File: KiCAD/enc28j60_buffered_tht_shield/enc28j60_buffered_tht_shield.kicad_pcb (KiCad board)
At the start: 2 copper layers, 68.6 x 53.3 mm, 8 parts, among them P1 Power, P2 Analog, P3 Digital, P4 Digital, P5 CONN_01X01, P6 CONN_01X01, P7 CONN_01X01, P8 CONN_01X01

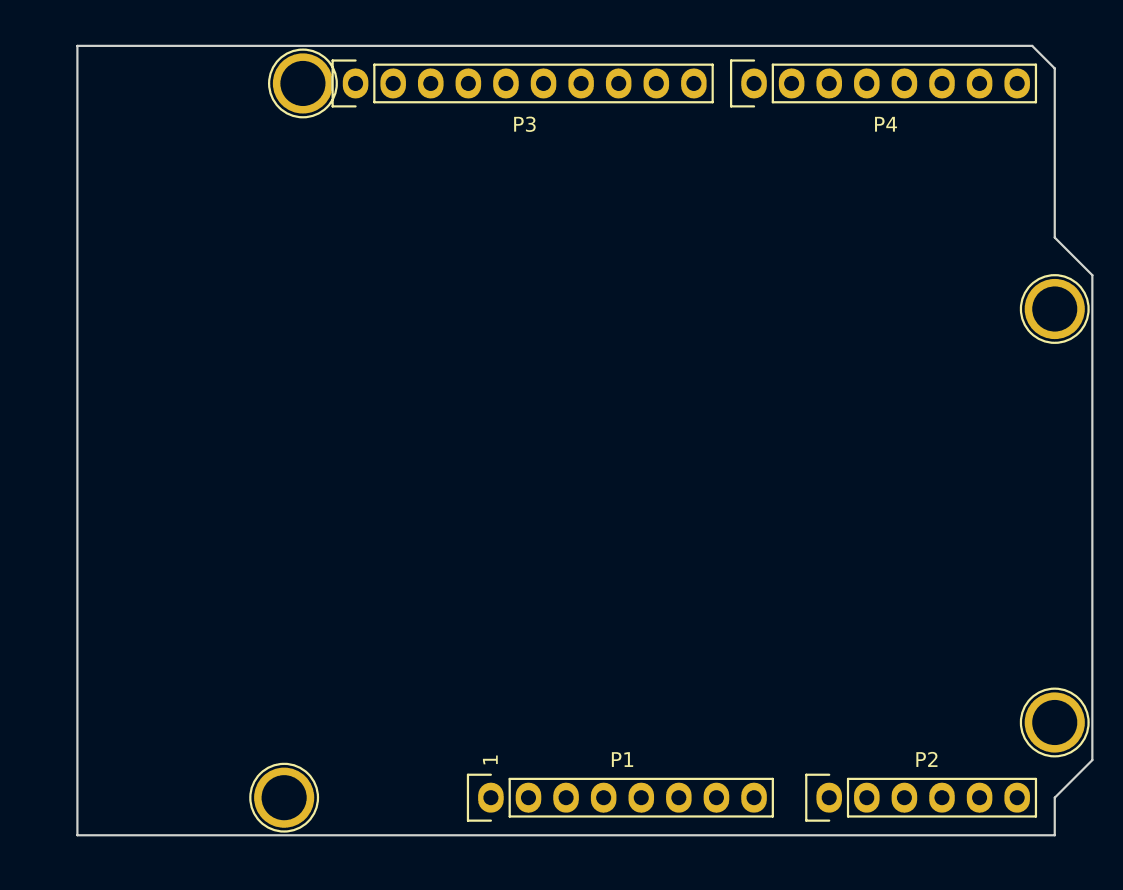
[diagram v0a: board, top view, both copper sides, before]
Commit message: Revision 1. 74HCT125N LM1117 3.3 ENC28J60
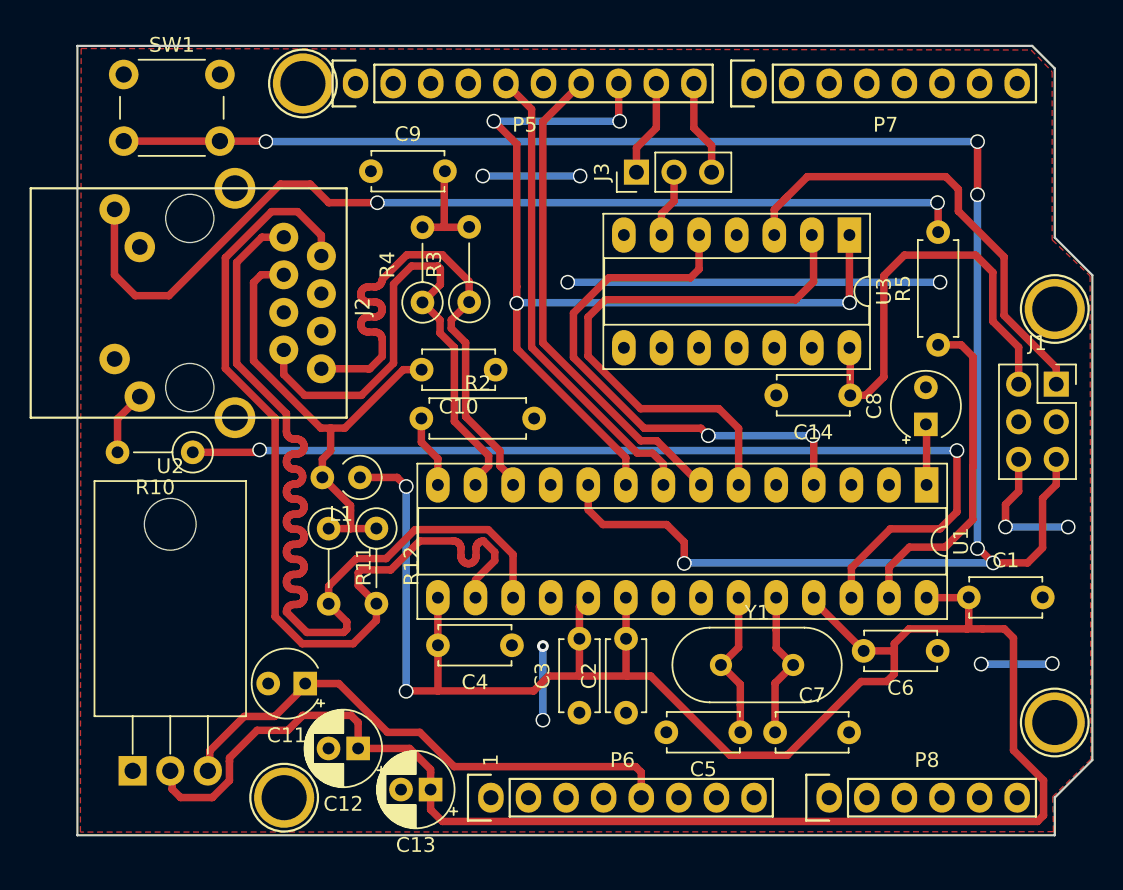
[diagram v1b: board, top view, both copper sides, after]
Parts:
- added C1: 100 nF, Capacitor_THT:C_Disc_D4.7mm_W2.5mm_P5.00mm, F.Cu at (171.2, 110.3)
- added C10: 100 nF, Capacitor_THT:C_Disc_D4.7mm_W2.5mm_P5.00mm, F.Cu at (139.3, 94.9)
- added C11: 10 μF ( Low ESR ), Capacitor_THT:CP_Radial_Tantal_D4.5mm_P2.50mm, F.Cu at (126.4, 116.1)
- added C12: 10 μF, Capacitor_THT:CP_Radial_D5.0mm_P2.00mm, F.Cu at (130.0, 120.5)
- added C13: 100 μF, Capacitor_THT:CP_Radial_D5.0mm_P2.00mm, F.Cu at (134.9, 123.3)
- added C14: 100 nF, Capacitor_THT:C_Disc_D4.7mm_W2.5mm_P5.00mm, F.Cu at (163.2, 96.6)
- added C2: 100 nF, Capacitor_THT:C_Disc_D4.7mm_W2.5mm_P5.00mm, F.Cu at (148.1, 118.1)
- added C3: 100 nF, Capacitor_THT:C_Disc_D4.7mm_W2.5mm_P5.00mm, F.Cu at (144.9, 118.1)
- added C4: 100 nF, Capacitor_THT:C_Disc_D4.7mm_W2.5mm_P5.00mm, F.Cu at (140.4, 113.5)
- added C5: 18 pF, Capacitor_THT:C_Disc_D4.7mm_W2.5mm_P5.00mm, F.Cu at (155.8, 119.4)
- added C6: 100 nF, Capacitor_THT:C_Disc_D4.7mm_W2.5mm_P5.00mm, F.Cu at (169.1, 113.9)
- added C7: 18 pF, Capacitor_THT:C_Disc_D4.7mm_W2.5mm_P5.00mm, F.Cu at (158.1, 119.4)
- added C8: 10 μF ( Low ESR ), Capacitor_THT:CP_Radial_Tantal_D4.5mm_P2.50mm, F.Cu at (168.3, 98.6)
- added C9: 100 nF, Capacitor_THT:C_Disc_D4.7mm_W2.5mm_P5.00mm, F.Cu at (130.8, 81.5)
- added J1: AVR-ISP-6, Connector_PinSocket_2.54mm:PinSocket_2x03_P2.54mm_Vertical, F.Cu at (177.1, 95.9)
- added J2: RJ45_MagJack_LMJTAB881X43M-L, RJ45_MagJack_LMJTAB881X43M-L:RJ45_MagJack_LMJTAB881X43M-L, F.Cu at (124.9, 86.0)
- added J3: Conn_01x03_Male, Connector_PinHeader_2.54mm:PinHeader_1x03_P2.54mm_Vertical, F.Cu at (148.8, 81.6)
- added L1: 4 μH, Inductor_THT:L_Axial_L6.6mm_D2.7mm_P2.54mm_Vertical_Vishay_IM-2, F.Cu at (130.1, 102.2)
- added R10: 180 Ω, Resistor_THT:R_Axial_DIN0207_L6.3mm_D2.5mm_P5.08mm_Vertical, F.Cu at (118.8, 100.5)
- added R11: 49.9 Ω 1%, Resistor_THT:R_Axial_DIN0207_L6.3mm_D2.5mm_P5.08mm_Vertical, F.Cu at (128.0, 105.6)
- added R12: 49.9 Ω 1%, Resistor_THT:R_Axial_DIN0207_L6.3mm_D2.5mm_P5.08mm_Vertical, F.Cu at (131.2, 105.6)
- added R2: 2.32 kΩ 1%, Resistor_THT:R_Axial_DIN0207_L6.3mm_D2.5mm_P7.62mm_Horizontal, F.Cu at (134.2, 98.2)
- added R3: 49.9 Ω 1%, Resistor_THT:R_Axial_DIN0207_L6.3mm_D2.5mm_P5.08mm_Vertical, F.Cu at (137.5, 90.3)
- added R4: 49.9 Ω 1%, Resistor_THT:R_Axial_DIN0207_L6.3mm_D2.5mm_P5.08mm_Vertical, F.Cu at (134.3, 90.4)
- added R5: 180 Ω, Resistor_THT:R_Axial_DIN0207_L6.3mm_D2.5mm_P7.62mm_Horizontal, F.Cu at (169.2, 93.2)
- added SW1: SW_Push, Button_Switch_THT:SW_PUSH_6mm_H5mm, F.Cu at (114.1, 75.0)
- added U1: ENC28J60x-SP, Package_DIP:DIP-28_W7.62mm_Socket_LongPads, F.Cu at (168.4, 102.7)
- added U2: LM1117-3.3, Package_TO_SOT_THT:TO-220-3_Horizontal_TabDown, F.Cu at (114.7, 122.0)
- added U3: 74HCT125N, Package_DIP:DIP-14_W7.62mm_Socket_LongPads, F.Cu at (163.2, 85.8)
- added Y1: 25 MHz, Crystal:Crystal_HC49-4H_Vertical, F.Cu at (154.5, 114.9)
- renumbered P5 to P1, P6 to P2, P7 to P3, P8 to P4, P3 to P5, P1 to P6, P4 to P7, P2 to P8
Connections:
- P5 pad 10: (no net) -> /8
- P5 pad 5: (no net) -> /13(SCK)
- P5 pad 6: (no net) -> /12(MISO)
- P5 pad 7: (no net) -> /11(**/MOSI)
- P5 pad 8: (no net) -> /10(**/SS)
- P5 pad 9: (no net) -> /9(**)
- P6 pad 3: (no net) -> /Reset
- P6 pad 4: (no net) -> +3V3
- P6 pad 5: (no net) -> +5V
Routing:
- net +3V3: track 0.00 -> 177.9 mm, vias 0 -> 2
- net /Reset: track 0.00 -> 128.2 mm, vias 0 -> 6
- net /LEDB: track 0.00 -> 67.0 mm, vias 0 -> 2
- net /10(**/SS): track 0.00 -> 66.4 mm, vias 0 -> 4
- net Net-(J2-Pad9): track 0.00 -> 66.3 mm, vias 0 -> 2
- net +5V: track 0.00 -> 66.3 mm
- net /TPOUT-: track 0.00 -> 63.7 mm
- net /TPOUT+: track 0.00 -> 63.6 mm
- net GND: track 0.00 -> 50.8 mm, vias 0 -> 10
- net /MISO_ENC: track 0.00 -> 38.1 mm
- net /TPIN-: track 0.00 -> 37.4 mm
- net /TPIN+: track 0.00 -> 37.0 mm
- net /INT_ENC: track 0.00 -> 36.8 mm, vias 0 -> 2
- net Net-(C10-Pad2): track 0.00 -> 33.5 mm
- net /11(**/MOSI): track 0.00 -> 33.3 mm
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- added copper zone on F.Cu, net GND
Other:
- net class Default: clearance 0.2 -> 0.254; trace_width 0.25 -> 0.508; via_dia 0.6 -> 0.8
- rule pad_to_mask_clearance: 0 -> 0.051
- rule trace_clearance: 0.2 -> 0.254

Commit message: Fixed AVR-ISP-PINS
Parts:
- moved U2 0.77 mm to (114.0, 122.1)
- moved C12 0.63 mm to (129.6, 120.0)
- moved R10 0.59 mm to (119.3, 100.7)
- moved C11 0.46 mm to (125.9, 116.0)
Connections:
- U1 pad 3: GND -> (no net)
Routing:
- net GND: track 50.8 -> 24.6 mm
- net +3V3: track 177.9 -> 173.5 mm
- net /12(MISO): track 31.6 -> 28.5 mm
- net /Reset: track 128.2 -> 126.4 mm
- net +5V: track 66.3 -> 64.7 mm
- net Net-(C10-Pad2): track 33.5 -> 34.4 mm
- net /LEDB: track 67.0 -> 66.1 mm
- net /MISO_ENC: track 38.1 -> 37.4 mm
- added copper zone on B.Cu, net GND

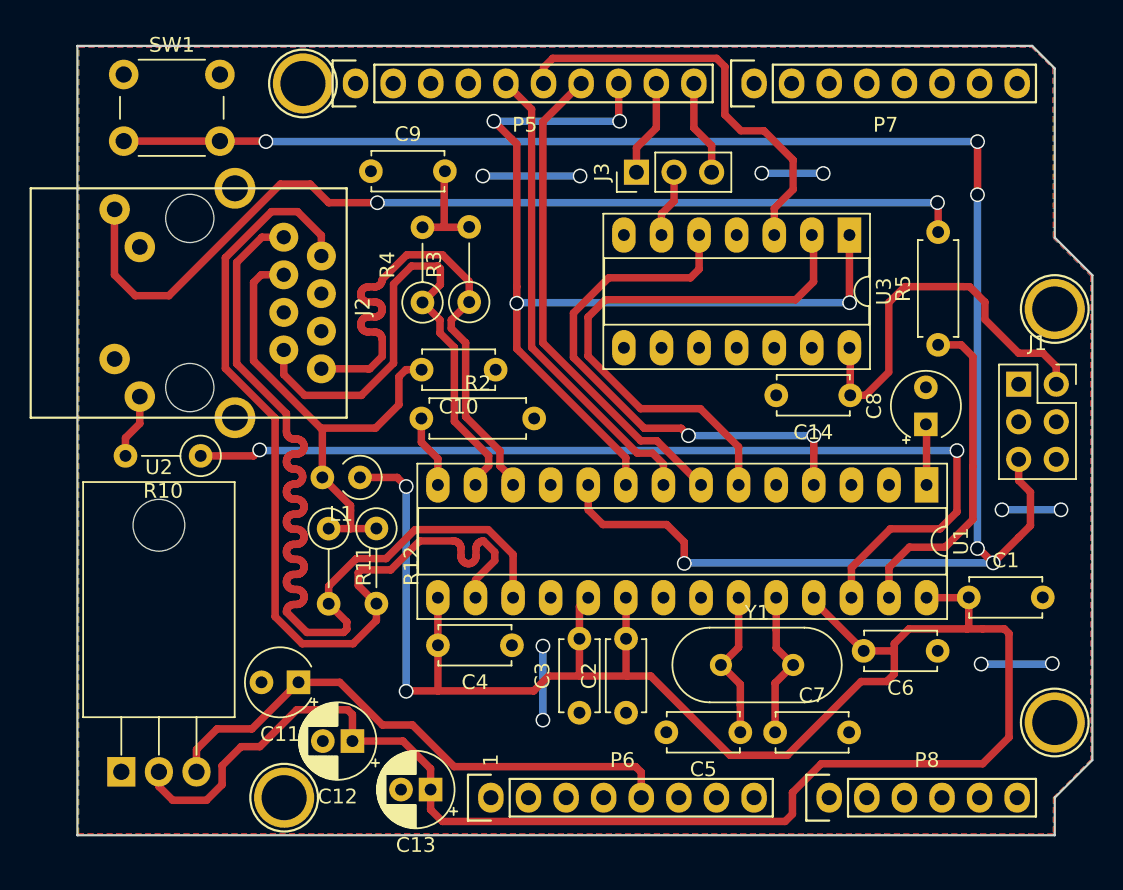
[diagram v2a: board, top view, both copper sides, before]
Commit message: Added LM117 DataSheet
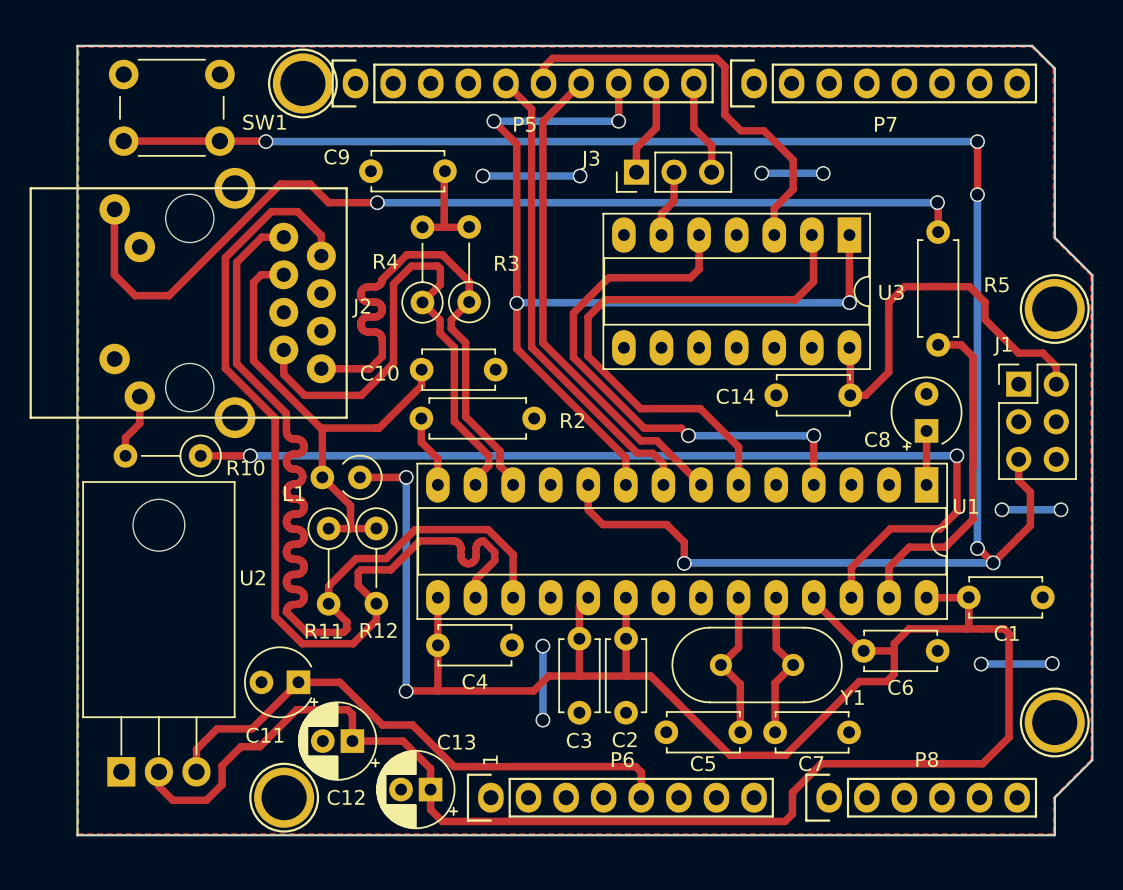
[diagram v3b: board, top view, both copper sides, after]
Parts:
- moved C8 0.45 mm to (168.4, 99.0)
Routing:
- net /LEDB: track 66.1 -> 65.6 mm
- removed copper zone on B.Cu, net GND
